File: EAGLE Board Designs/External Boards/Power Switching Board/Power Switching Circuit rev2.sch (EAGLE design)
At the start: 59 parts, among them J1 CONNECTOR-3_, J2 CONNECTOR-4_SOURIAU_, J3 CONNECTOR-4_SOURIAU_, K1 J115F11A6, Q1 TK100S04N1L, Q2 TK100S04N1L, Q3 TK100S04N1L, Q4 TK100S04N1L, U1 LTC4421

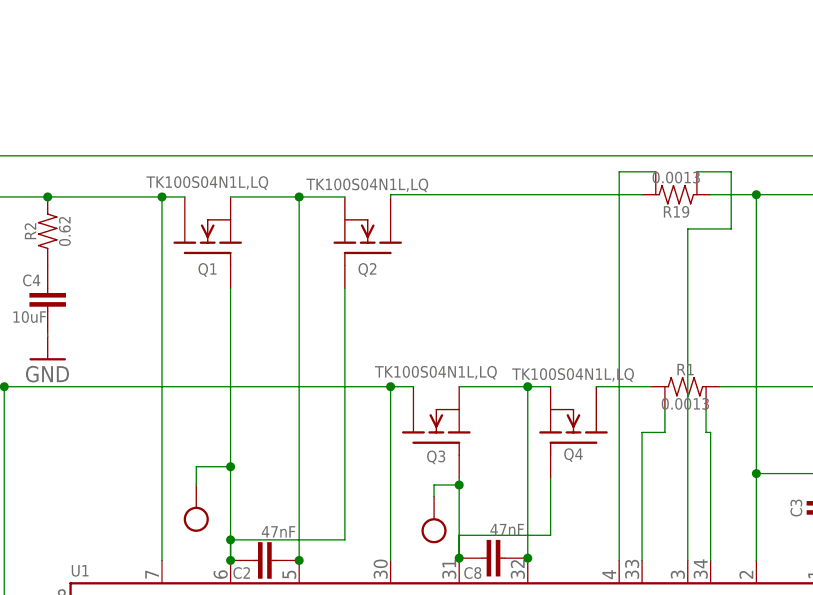
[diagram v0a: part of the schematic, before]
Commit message: Replaced mosfets with new device in new library
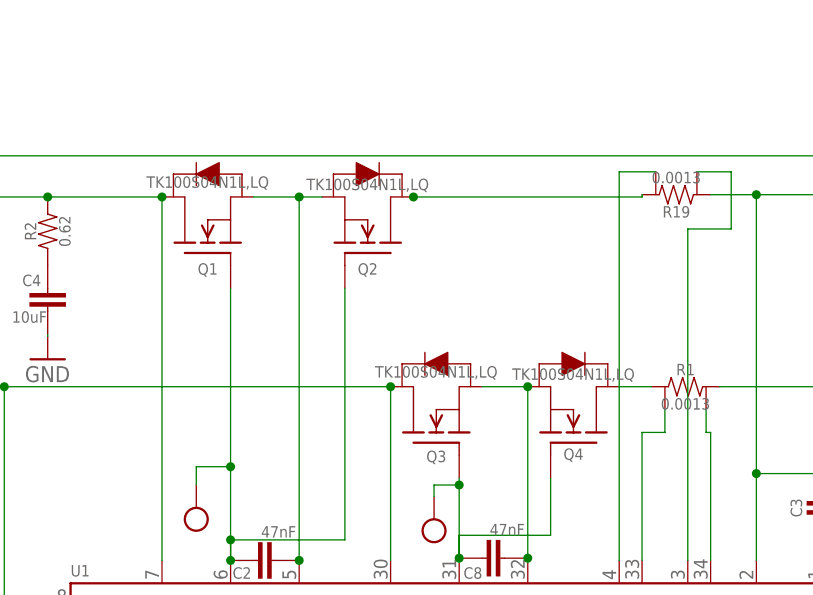
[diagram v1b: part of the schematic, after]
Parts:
- Q1, Q2, Q3, Q4: value TK100S04N1L -> TRANSISTOR_N_MOS_2-7K1S_TK100S04N1L,LQ; device HyTechDevices:TK100S04N1L -> HyTechDevices:TRANSISTOR_N_MOS_2-7K1S_TK100S04N1L,LQ
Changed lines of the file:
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@@
 <part name="R17" library="HyTechDevices" deviceset="RESISTOR" device="0603" value="10k"/>
 <part name="R19" library="HyTechDevices" deviceset="RESISTOR_SENSE" device=""/>
-<part name="Q1" library="HyTechDevices" deviceset="TK100S04N1L" device=""/>
-<part name="Q2" library="HyTechDevices" deviceset="TK100S04N1L" device=""/>
-<part name="Q4" library="HyTechDevices" deviceset="TK100S04N1L" device=""/>
-<part name="Q3" library="HyTechDevices" deviceset="TK100S04N1L" device=""/>
+<part name="Q1" library="HyTechDevices" deviceset="TRANSISTOR_N_MOS_?_*" device="2-7K1S" technology="TK100S04N1L,LQ"/>
+<part name="Q2" library="HyTechDevices" deviceset="TRANSISTOR_N_MOS_?_*" device="2-7K1S" technology="TK100S04N1L,LQ"/>
+<part name="Q4" library="HyTechDevices" deviceset="TRANSISTOR_N_MOS_?_*" device="2-7K1S" technology="TK100S04N1L,LQ"/>
+<part name="Q3" library="HyTechDevices" deviceset="TRANSISTOR_N_MOS_?_*" device="2-7K1S" technology="TK100S04N1L,LQ"/>
 <part name="RN2" library="HyTechDevices" deviceset="RESISTOR_NETWORK_4_*" device="" technology="10K"/>
 <part name="U$11" library="HyTechDevices" deviceset="TEST_POINT" device="MICRO_MINIATURE"/>
@@
 <pinref part="U1" gate="G$1" pin="V1"/>
 <wire x1="-20.828" y1="5.588" x2="-20.828" y2="45.974" width="0.1524" layer="91"/>
-<wire x1="-20.828" y1="45.974" x2="-18.288" y2="45.974" width="0.1524" layer="91"/>
 <wire x1="-20.828" y1="45.974" x2="-33.528" y2="45.974" width="0.1524" layer="91"/>
 <junction x="-20.828" y="45.974"/>
@@
 <pinref part="U1" gate="G$1" pin="SOURCE2"/>
 <wire x1="19.812" y1="5.842" x2="19.812" y2="5.588" width="0.1524" layer="91"/>
-<wire x1="12.192" y1="24.892" x2="19.812" y2="24.892" width="0.1524" layer="91"/>
-<wire x1="19.812" y1="24.892" x2="22.352" y2="24.892" width="0.1524" layer="91"/>
+<wire x1="14.732" y1="24.892" x2="19.812" y2="24.892" width="0.1524" layer="91"/>
 <wire x1="19.812" y1="5.842" x2="19.812" y2="24.892" width="0.1524" layer="91"/>
 <junction x="19.812" y="5.842"/>
@@
 <pinref part="U1" gate="G$1" pin="V2"/>
 <wire x1="4.572" y1="5.588" x2="4.572" y2="24.892" width="0.1524" layer="91"/>
-<wire x1="4.572" y1="24.892" x2="7.112" y2="24.892" width="0.1524" layer="91"/>
 <wire x1="4.572" y1="24.892" x2="-38.354" y2="24.892" width="0.1524" layer="91"/>
 <junction x="4.572" y="24.892"/>
@@
 <pinref part="U1" gate="G$1" pin="SOURCE1"/>
 <pinref part="C2" gate="G$1" pin="1"/>
-<wire x1="-13.208" y1="45.974" x2="-5.588" y2="45.974" width="0.1524" layer="91"/>
-<wire x1="-5.588" y1="45.974" x2="-0.508" y2="45.974" width="0.1524" layer="91"/>
+<wire x1="-10.668" y1="45.974" x2="-5.588" y2="45.974" width="0.1524" layer="91"/>
+<wire x1="-5.588" y1="45.974" x2="-3.048" y2="45.974" width="0.1524" layer="91"/>
 <wire x1="-5.588" y1="5.588" x2="-5.588" y2="45.974" width="0.1524" layer="91"/>
 <junction x="-5.588" y="5.588"/>
@@
 <net name="N$5" class="0">
 <segment>
-<wire x1="27.432" y1="24.892" x2="33.528" y2="24.892" width="0.1524" layer="91"/>
+<wire x1="29.972" y1="24.892" x2="33.528" y2="24.892" width="0.1524" layer="91"/>
 <pinref part="R1" gate="G$1" pin="1"/>
 <pinref part="Q4" gate="G$1" pin="D"/>
@@
 <net name="N$8" class="0">
 <segment>
-<wire x1="32.512" y1="46.228" x2="4.572" y2="46.228" width="0.1524" layer="91"/>
-<wire x1="4.572" y1="46.228" x2="4.572" y2="45.974" width="0.1524" layer="91"/>
+<wire x1="7.112" y1="46.228" x2="7.112" y2="45.974" width="0.1524" layer="91"/>
+<pinref part="Q2" gate="G$1" pin="D"/>
 <pinref part="R19" gate="G$1" pin="2"/>
-<pinref part="Q2" gate="G$1" pin="D"/>
-</segment>
-</net>
+<wire x1="32.512" y1="46.228" x2="32.512" y2="45.974" width="0.1524" layer="91"/>
+<wire x1="32.512" y1="45.974" x2="7.112" y2="45.974" width="0.1524" layer="91"/>
+<junction x="7.112" y="45.974"/>
+</segment>
+</net>

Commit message: Revert "Replaced mosfets with new device in new library"
This reverts commit 47685a596586f3a57bfaa4732962c561ce9df098.
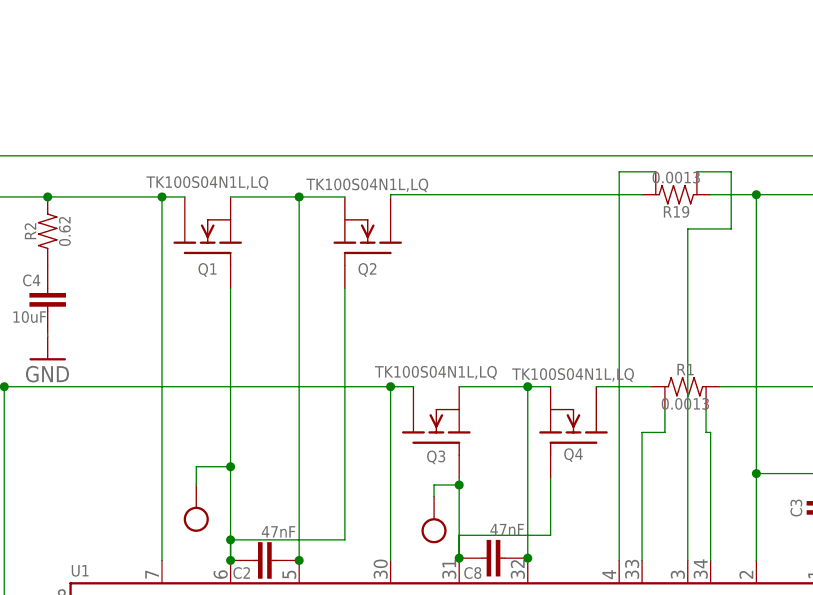
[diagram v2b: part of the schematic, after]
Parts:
- Q1, Q2, Q3, Q4: value TRANSISTOR_N_MOS_2-7K1S_TK100S04N1L,LQ -> TK100S04N1L; device HyTechDevices:TRANSISTOR_N_MOS_2-7K1S_TK100S04N1L,LQ -> HyTechDevices:TK100S04N1L
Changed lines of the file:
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@@
 <part name="R17" library="HyTechDevices" deviceset="RESISTOR" device="0603" value="10k"/>
 <part name="R19" library="HyTechDevices" deviceset="RESISTOR_SENSE" device=""/>
-<part name="Q1" library="HyTechDevices" deviceset="TRANSISTOR_N_MOS_?_*" device="2-7K1S" technology="TK100S04N1L,LQ"/>
-<part name="Q2" library="HyTechDevices" deviceset="TRANSISTOR_N_MOS_?_*" device="2-7K1S" technology="TK100S04N1L,LQ"/>
-<part name="Q4" library="HyTechDevices" deviceset="TRANSISTOR_N_MOS_?_*" device="2-7K1S" technology="TK100S04N1L,LQ"/>
-<part name="Q3" library="HyTechDevices" deviceset="TRANSISTOR_N_MOS_?_*" device="2-7K1S" technology="TK100S04N1L,LQ"/>
+<part name="Q1" library="HyTechDevices" deviceset="TK100S04N1L" device=""/>
+<part name="Q2" library="HyTechDevices" deviceset="TK100S04N1L" device=""/>
+<part name="Q4" library="HyTechDevices" deviceset="TK100S04N1L" device=""/>
+<part name="Q3" library="HyTechDevices" deviceset="TK100S04N1L" device=""/>
 <part name="RN2" library="HyTechDevices" deviceset="RESISTOR_NETWORK_4_*" device="" technology="10K"/>
 <part name="U$11" library="HyTechDevices" deviceset="TEST_POINT" device="MICRO_MINIATURE"/>
@@
 <pinref part="U1" gate="G$1" pin="V1"/>
 <wire x1="-20.828" y1="5.588" x2="-20.828" y2="45.974" width="0.1524" layer="91"/>
+<wire x1="-20.828" y1="45.974" x2="-18.288" y2="45.974" width="0.1524" layer="91"/>
 <wire x1="-20.828" y1="45.974" x2="-33.528" y2="45.974" width="0.1524" layer="91"/>
 <junction x="-20.828" y="45.974"/>
@@
 <pinref part="U1" gate="G$1" pin="SOURCE2"/>
 <wire x1="19.812" y1="5.842" x2="19.812" y2="5.588" width="0.1524" layer="91"/>
-<wire x1="14.732" y1="24.892" x2="19.812" y2="24.892" width="0.1524" layer="91"/>
+<wire x1="12.192" y1="24.892" x2="19.812" y2="24.892" width="0.1524" layer="91"/>
+<wire x1="19.812" y1="24.892" x2="22.352" y2="24.892" width="0.1524" layer="91"/>
 <wire x1="19.812" y1="5.842" x2="19.812" y2="24.892" width="0.1524" layer="91"/>
 <junction x="19.812" y="5.842"/>
@@
 <pinref part="U1" gate="G$1" pin="V2"/>
 <wire x1="4.572" y1="5.588" x2="4.572" y2="24.892" width="0.1524" layer="91"/>
+<wire x1="4.572" y1="24.892" x2="7.112" y2="24.892" width="0.1524" layer="91"/>
 <wire x1="4.572" y1="24.892" x2="-38.354" y2="24.892" width="0.1524" layer="91"/>
 <junction x="4.572" y="24.892"/>
@@
 <pinref part="U1" gate="G$1" pin="SOURCE1"/>
 <pinref part="C2" gate="G$1" pin="1"/>
-<wire x1="-10.668" y1="45.974" x2="-5.588" y2="45.974" width="0.1524" layer="91"/>
-<wire x1="-5.588" y1="45.974" x2="-3.048" y2="45.974" width="0.1524" layer="91"/>
+<wire x1="-13.208" y1="45.974" x2="-5.588" y2="45.974" width="0.1524" layer="91"/>
+<wire x1="-5.588" y1="45.974" x2="-0.508" y2="45.974" width="0.1524" layer="91"/>
 <wire x1="-5.588" y1="5.588" x2="-5.588" y2="45.974" width="0.1524" layer="91"/>
 <junction x="-5.588" y="5.588"/>
@@
 <net name="N$5" class="0">
 <segment>
-<wire x1="29.972" y1="24.892" x2="33.528" y2="24.892" width="0.1524" layer="91"/>
+<wire x1="27.432" y1="24.892" x2="33.528" y2="24.892" width="0.1524" layer="91"/>
 <pinref part="R1" gate="G$1" pin="1"/>
 <pinref part="Q4" gate="G$1" pin="D"/>
@@
 <net name="N$8" class="0">
 <segment>
-<wire x1="7.112" y1="46.228" x2="7.112" y2="45.974" width="0.1524" layer="91"/>
+<wire x1="32.512" y1="46.228" x2="4.572" y2="46.228" width="0.1524" layer="91"/>
+<wire x1="4.572" y1="46.228" x2="4.572" y2="45.974" width="0.1524" layer="91"/>
+<pinref part="R19" gate="G$1" pin="2"/>
 <pinref part="Q2" gate="G$1" pin="D"/>
-<pinref part="R19" gate="G$1" pin="2"/>
-<wire x1="32.512" y1="46.228" x2="32.512" y2="45.974" width="0.1524" layer="91"/>
-<wire x1="32.512" y1="45.974" x2="7.112" y2="45.974" width="0.1524" layer="91"/>
-<junction x="7.112" y="45.974"/>
-</segment>
-</net>
+</segment>
+</net>
